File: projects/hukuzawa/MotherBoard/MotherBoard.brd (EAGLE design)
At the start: 75 x 55 mm, 27 parts, among them IC1 PIC16F886, Q1 CERALOCK

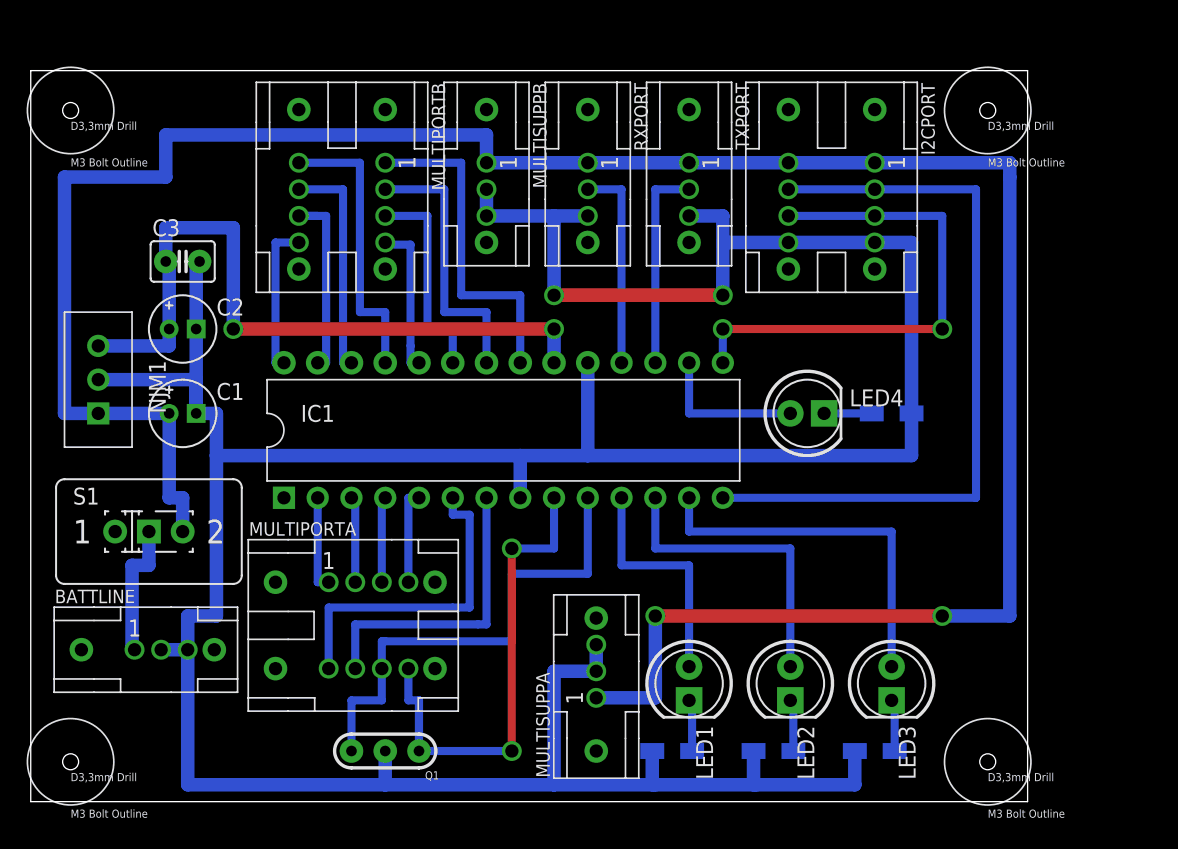
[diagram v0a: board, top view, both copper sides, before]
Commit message: マザーボード修正
一部文字の見えにくい部分を修正
PICのライブラリの重大な問題を修正
回路図・ボード図をpng,pdfにエクスポート
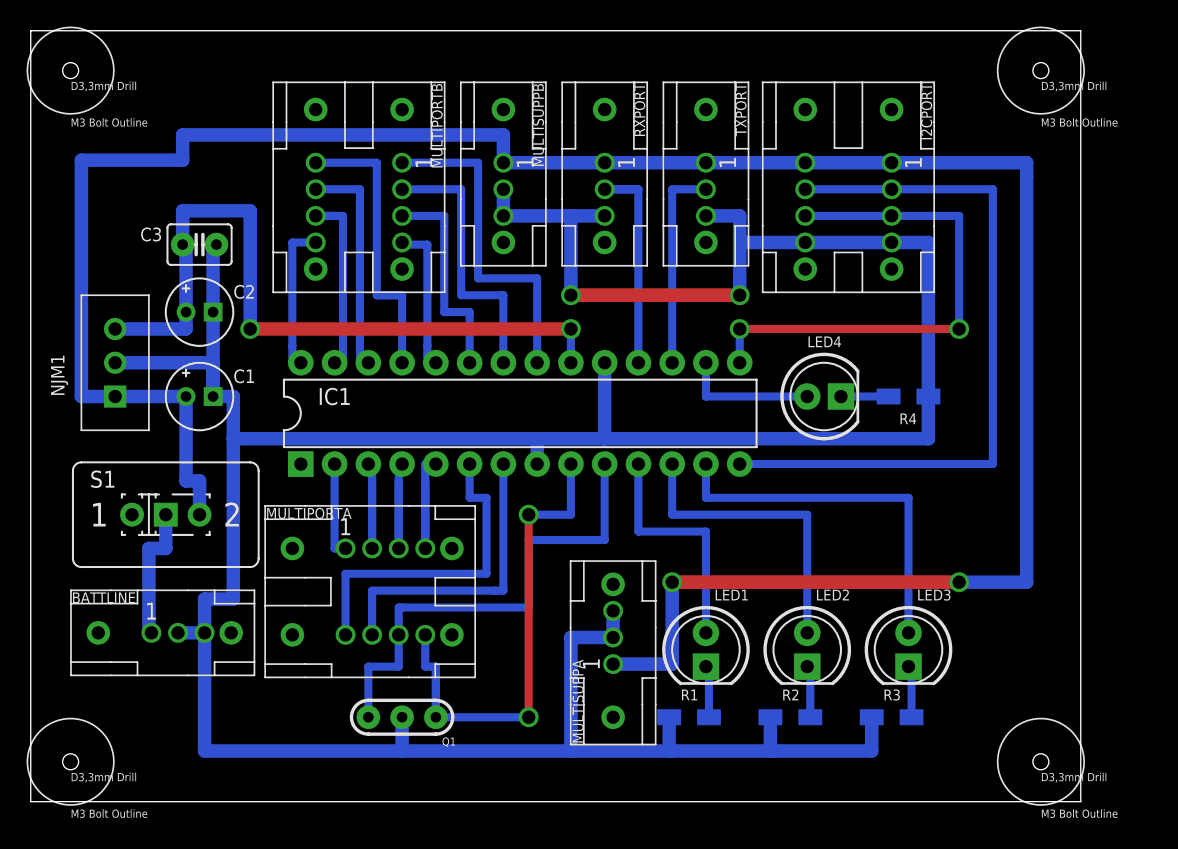
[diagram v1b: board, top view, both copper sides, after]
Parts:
- moved HOLE3 5.00 mm to (76.0, 55.0)
- moved HOLE4 4.00 mm to (76.0, 3.00)
- moved HOLE2 3.00 mm to (3.00, 55.0)
- moved LED3 2.84 mm to (66.0, 11.4)
- moved R1 2.84 mm to (49.5, 6.35)
- moved LED2 2.84 mm to (58.4, 11.4)
- moved Q1 2.84 mm to (27.9, 6.35)
- moved MULTIPORTA 2.84 mm to (19.7, 19.1)
- moved MULTISUPPA 2.84 mm to (43.8, 6.35)
- moved R2 2.84 mm to (57.1, 6.35)
- moved R3 2.84 mm to (64.8, 6.35)
- moved LED1 2.84 mm to (50.8, 11.4)
- moved R4 1.80 mm to (66.0, 30.5)
- moved NJM1 1.80 mm to (6.35, 33.0)
- moved BATTLINE 1.80 mm to (5.08, 12.7)
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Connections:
- net A0: now also IC1.2; no longer IC1.02
- net A1: now also IC1.3; no longer IC1.03
- net A2: now also IC1.4; no longer IC1.04
- net A3: now also IC1.5; no longer IC1.05
- net A4: now also IC1.6; no longer IC1.06
- net A5: now also IC1.7; no longer IC1.07
- net A7: now also IC1.9; no longer IC1.09
- net GND: now also IC1.8; no longer IC1.08
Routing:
- net GND: track 259.4 -> 254.3 mm
- net A3: track 7.14 -> 12.2 mm
- net A2: track 6.61 -> 11.7 mm
- net A1: track 6.63 -> 11.7 mm
- net V+: track 183.3 -> 179.5 mm
- net SCL: track 56.4 -> 53.8 mm
- net RX: track 15.6 -> 18.1 mm
- net B4: track 21.5 -> 23.5 mm
- net +5V: track 53.8 -> 55.1 mm
- net OPRLED: track 11.4 -> 10.2 mm
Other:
- board size 75 x 55 mm -> 79 x 58 mm

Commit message: マザーボード修正
3.3mm穴がショートしないよう修正
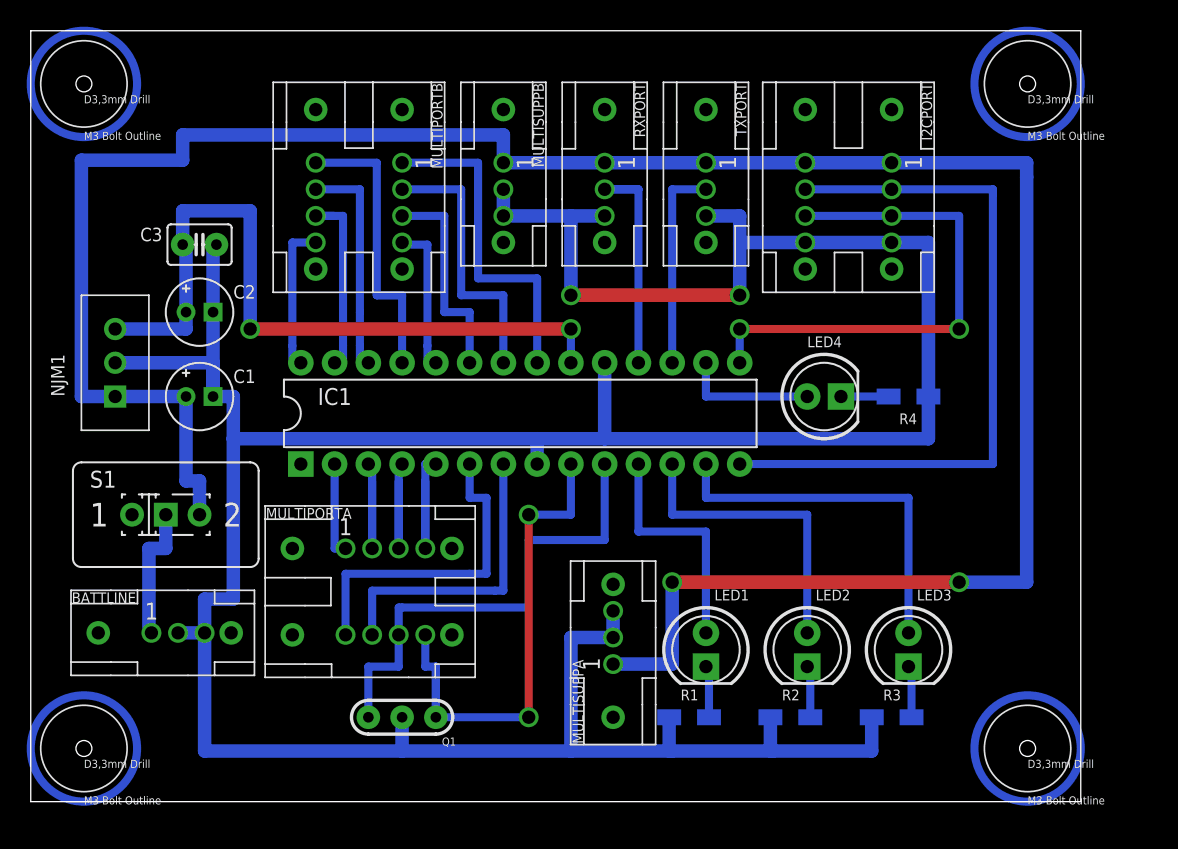
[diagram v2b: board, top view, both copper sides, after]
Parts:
- HOLE1, HOLE2, HOLE3, HOLE4: device FP-21T for MITS:HOLE3.3 -> Hole:HOLE3.3
- moved HOLE1 1.41 mm to (4.00, 4.00)
- moved HOLE2 1.41 mm to (4.00, 54.0)
- moved HOLE3 1.41 mm to (75.0, 54.0)
- moved HOLE4 1.41 mm to (75.0, 4.00)
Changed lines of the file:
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@@
 <setting verticaltext="up"/>
 </settings>
-<grid distance="50" unitdist="mil" unit="mil" style="lines" multiple="2" display="yes" altdistance="25" altunitdist="mil" altunit="mil"/>
+<grid distance="0.5" unitdist="mm" unit="mm" style="lines" multiple="2" display="yes" altdistance="25" altunitdist="mil" altunit="mil"/>
 <layers>
 <layer number="1" name="Top" color="4" fill="1" visible="yes" active="yes"/>
@@
 <attribute name="VALUE" x="47.045" y="4.35" size="0.8128" layer="27" rot="R90"/>
 </element>
-<element name="HOLE4" library="FP-21T for MITS" package="HOLE3.3" value="HOLE3.3M3BOLT" x="76" y="3"/>
-<element name="HOLE3" library="FP-21T for MITS" package="HOLE3.3" value="HOLE3.3M3BOLT" x="76" y="55"/>
-<element name="HOLE2" library="FP-21T for MITS" package="HOLE3.3" value="HOLE3.3M3BOLT" x="3" y="55"/>
-<element name="HOLE1" library="FP-21T for MITS" package="HOLE3.3" value="HOLE3.3M3BOLT" x="3" y="3"/>
 <element name="IC1" library="PIC" package="DIL28" value="PIC16F886" x="36.83" y="29.21"/>
+<element name="HOLE4" library="Hole" package="HOLE3.3" value="HOLE3.3M3BOLT" x="75" y="4"/>
+<element name="HOLE3" library="Hole" package="HOLE3.3" value="HOLE3.3M3BOLT" x="75" y="54"/>
+<element name="HOLE2" library="Hole" package="HOLE3.3" value="HOLE3.3M3BOLT" x="4" y="54"/>
+<element name="HOLE1" library="Hole" package="HOLE3.3" value="HOLE3.3M3BOLT" x="4" y="4"/>
 </elements>
 <signals>

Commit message: マザーボード回路修正
配置の見直し・再配線
使用ライブラリの更新
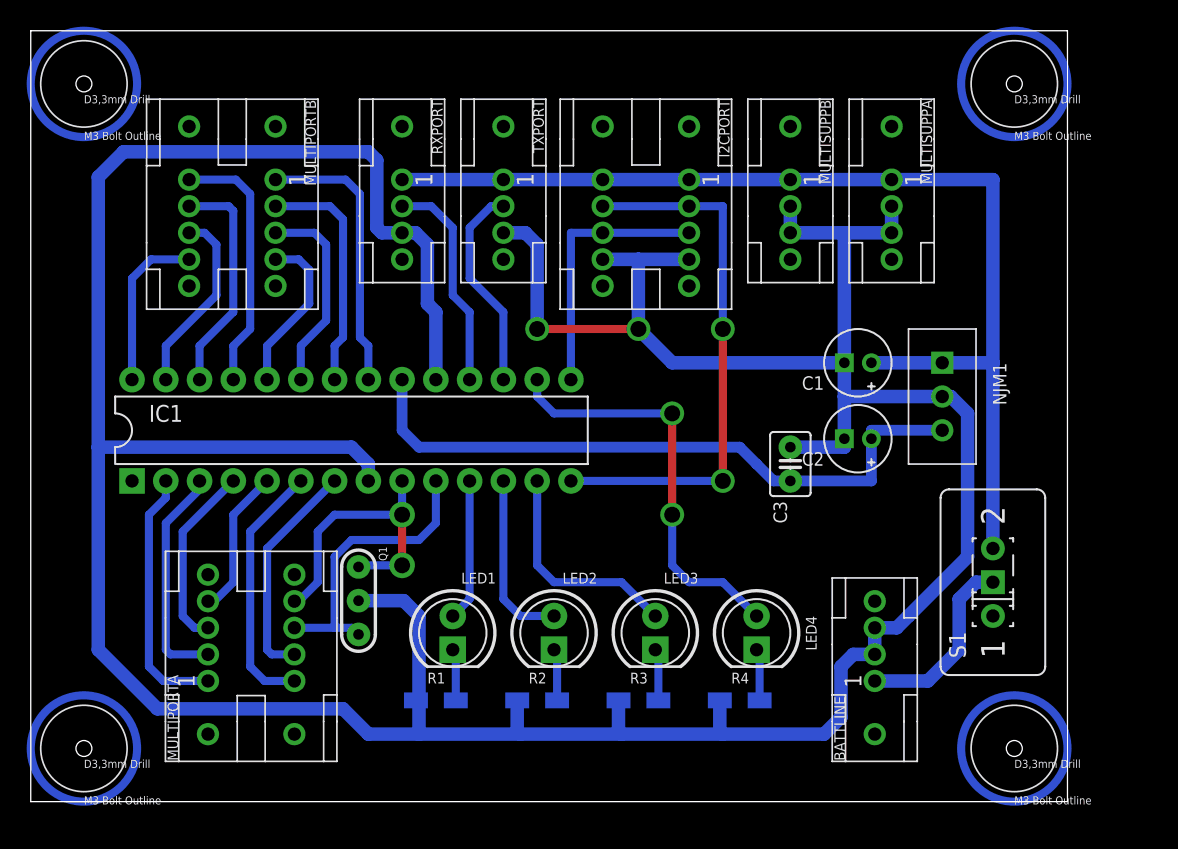
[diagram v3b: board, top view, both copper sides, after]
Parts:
- moved S1 62.4 mm to (72.4, 16.5), turned to 90 degrees
- moved NJM1 62.3 mm to (68.6, 30.5), turned to 270 degrees
- moved BATTLINE 58.9 mm to (63.5, 5.08), turned to 0 degrees
- moved C2 50.4 mm to (62.2, 27.3), turned to 180 degrees
- moved C1 49.6 mm to (62.2, 33.0), turned to 180 degrees
- moved MULTISUPPA 49.1 mm to (64.8, 50.8), turned to 180 degrees
- moved C3 47.4 mm to (57.1, 25.4), turned to 90 degrees
- moved R4 26.2 mm to (53.3, 7.62), turned to 0 degrees
- moved MULTISUPPB 21.6 mm to (57.1, 50.8)
- moved LED2 19.1 mm to (39.4, 12.7)
- moved LED3 19.1 mm to (47.0, 12.7)
- moved R1 19.1 mm to (30.5, 7.62)
- moved LED1 19.1 mm to (31.8, 12.7)
- moved R2 19.1 mm to (38.1, 7.62)
- moved R3 19.1 mm to (45.7, 7.62)
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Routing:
- net V+: track 179.5 -> 81.3 mm, vias 2 -> 0
- net GND: track 254.3 -> 296.5 mm
- net OPRLED: track 10.2 -> 31.3 mm, vias 0 -> 2
- net SDA: track 39.1 -> 19.9 mm, vias 2 -> 0
- net A7: track 40.0 -> 22.7 mm
- net A6: track 36.8 -> 22.2 mm
- net SCL: track 53.8 -> 41.1 mm, vias 0 -> 2
- net A0: track 7.17 -> 19.4 mm
- net LED2: track 27.9 -> 16.8 mm
- net LED1: track 22.9 -> 13.2 mm
- net LED0: track 17.8 -> 10.7 mm
- net A5: track 22.7 -> 17.0 mm
- net A4: track 24.7 -> 19.3 mm
- net A1: track 11.7 -> 17.1 mm
- net +5V: track 55.1 -> 49.8 mm, vias 2 -> 0
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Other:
- board size 79 x 58 mm -> 78 x 58 mm

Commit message: マザーボード回路ver1.20
ポート部分仕様変更
再配置・再配線
回路基板サイズの縮小
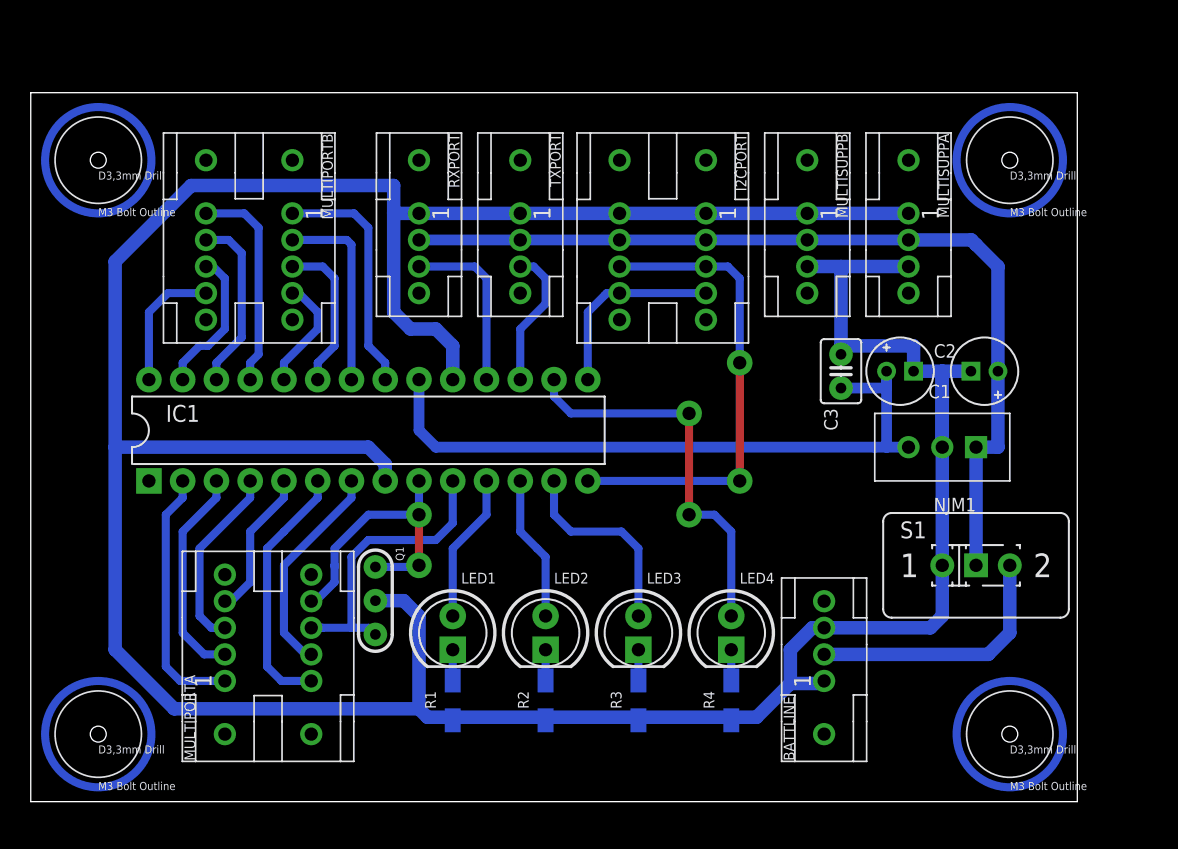
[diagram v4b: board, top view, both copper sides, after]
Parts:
- moved C1 9.55 mm to (71.8, 32.4)
- moved C3 7.96 mm to (61.0, 32.4)
- moved C2 5.99 mm to (65.4, 32.4), turned to 0 degrees
- moved HOLE2 5.84 mm to (5.08, 48.3)
- moved HOLE3 5.75 mm to (73.7, 48.3)
- moved BATTLINE 3.81 mm to (59.7, 5.08)
- moved NJM1 3.81 mm to (68.6, 26.7), turned to 180 degrees
- moved MULTISUPPA 2.84 mm to (66.0, 48.3)
- moved MULTISUPPB 2.84 mm to (58.4, 48.3)
- moved MULTIPORTB 2.84 mm to (19.7, 48.3)
- moved RXPORT 2.84 mm to (29.2, 48.3)
- moved I2CPORT 2.84 mm to (50.8, 48.3)
- moved TXPORT 2.84 mm to (36.8, 48.3)
- moved LED4 1.91 mm to (52.7, 12.7)
- moved S1 1.80 mm to (71.1, 17.8), turned to 0 degrees
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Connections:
- removed net 9VLINE: BATTLINE.1-1, S1.2
- new net BATTLINE: BATTLINE.1-2, S1.3
- net GND: now also BATTLINE.1-1, I2CPORT.1-1, I2CPORT.2-1, MULTISUPPA.1-1, MULTISUPPB.1-1, RXPORT.1-1, S1.1, TXPORT.1-1; no longer BATTLINE.1-2, I2CPORT.1-4, I2CPORT.2-4, MULTISUPPA.1-2, MULTISUPPB.1-2, RXPORT.1-3, TXPORT.1-3
- net RX: now also RXPORT.1-3; no longer RXPORT.1-2
- net SCL: now also I2CPORT.1-3, I2CPORT.2-3; no longer I2CPORT.1-2, I2CPORT.2-2
- net SDA: now also I2CPORT.1-4, I2CPORT.2-4; no longer I2CPORT.1-3, I2CPORT.2-3
- net TX: now also TXPORT.1-3; no longer TXPORT.1-2
- net V+: now also I2CPORT.1-2, I2CPORT.2-2, MULTISUPPA.1-2, MULTISUPPB.1-2, RXPORT.1-2, S1.2, TXPORT.1-2; no longer I2CPORT.1-1, I2CPORT.2-1, MULTISUPPA.1-1, MULTISUPPB.1-1, RXPORT.1-1, S1.3, TXPORT.1-1
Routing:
- net GND: track 296.5 -> 264.2 mm, vias 2 -> 0
- net BATTLINE: track 0.00 -> 19.7 mm
- net 9VLINE: track 14.2 -> 0.00 mm
- net V+: track 81.3 -> 68.5 mm
- net SDA: track 19.9 -> 14.6 mm
- net SCL: track 41.1 -> 36.1 mm
- net TX: track 15.7 -> 10.7 mm
- net B5: track 17.2 -> 13.4 mm
- net B3: track 12.4 -> 8.63 mm
- net B4: track 19.5 -> 16.1 mm
- net B2: track 15.1 -> 11.7 mm
- net RX: track 16.4 -> 13.1 mm
- net B1: track 17.8 -> 14.7 mm
- net B6: track 14.2 -> 11.1 mm
- net B0: track 21.0 -> 18.1 mm
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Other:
- board size 78 x 58 mm -> 78.7 x 53.3 mm
